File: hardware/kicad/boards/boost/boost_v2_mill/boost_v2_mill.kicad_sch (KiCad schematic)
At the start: 17 parts, among them J1 lager ind (5V), J2 V2 ud (10V), J3 PWM (isoleret), J4 drive +15V, M1 IRF530, U1 CNY17, U2 IR2110

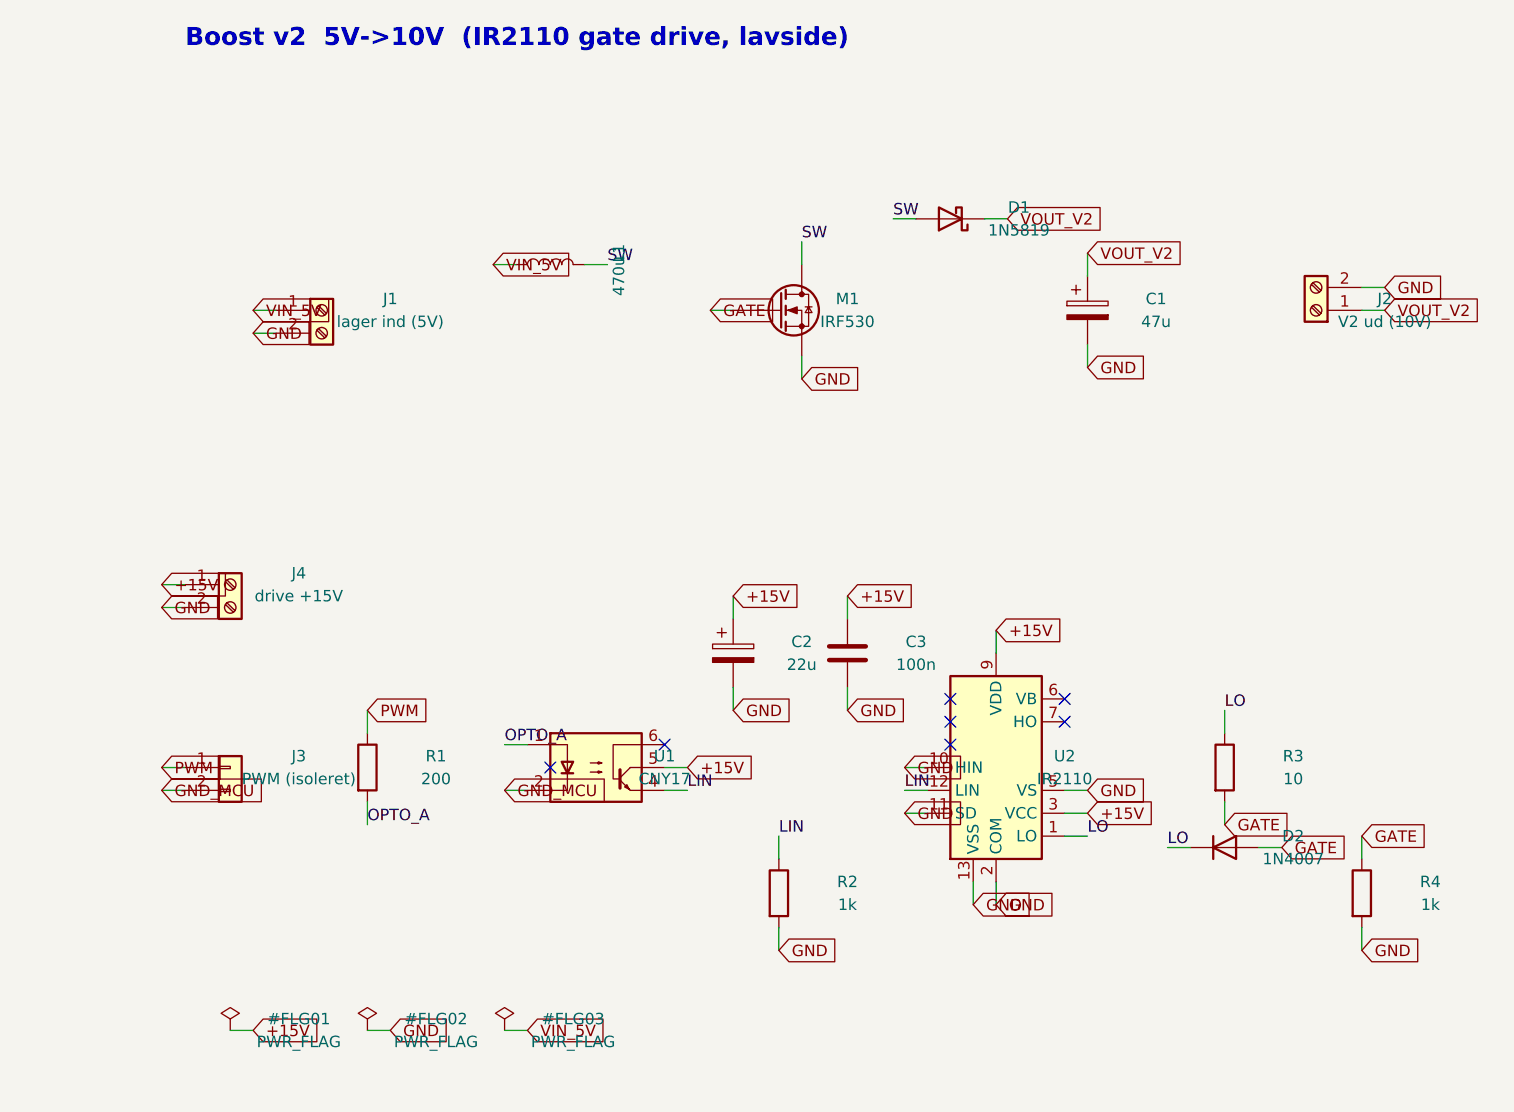
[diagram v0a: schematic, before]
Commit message: system PCB: lock double-sided CNC integration (Phase 0-2.2)
Set up the whole-system board as one double-sided CNC-milled PCB.

- system.kicad_pro: CNC double-sided netclass (clearance 1.0 mm, track 1.0 mm,
  hand-stitch via 2.4/1.0 mm) replacing the laser 0.8 mm rules
- interface contract (docs/superpowers/specs/2026-06-27-...) + rewritten
  label howto for the 5-board split-MCU integration
- split MCU: Arduino owns MPPT (PV INA219 + drives mppt_buck PWM at 5 V),
  C2000 runs motor-buck + boost PID; the two MCUs are fully independent
- current_sense (discrete) dropped; current sensing via PV INA219
- c2000_feedback: strip I-channels + PWM pass, keep 3 V-dividers
  (V1/LOAD/STORE -> ADC)
- hierarchical labels placed on the 5 boards (motor_power, motor_feedback,
  mppt_buck, boost_v2_mill, c2000_feedback) for the system top sheet
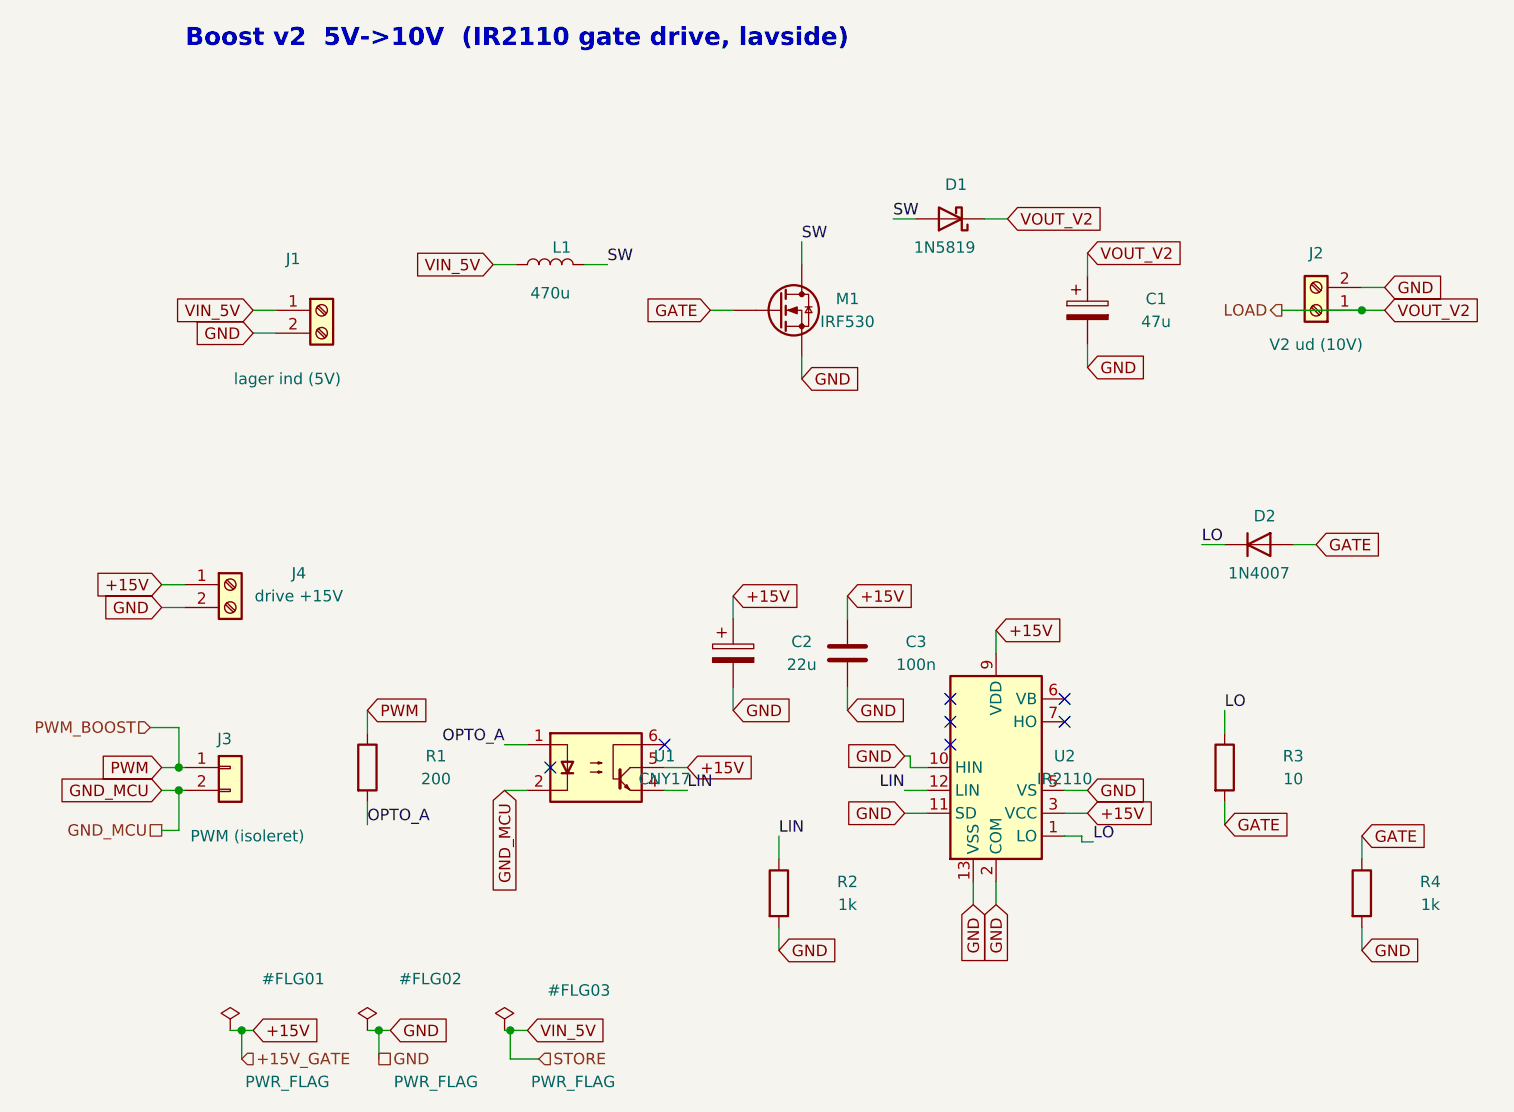
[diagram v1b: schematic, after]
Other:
- moved on the sheet: D2

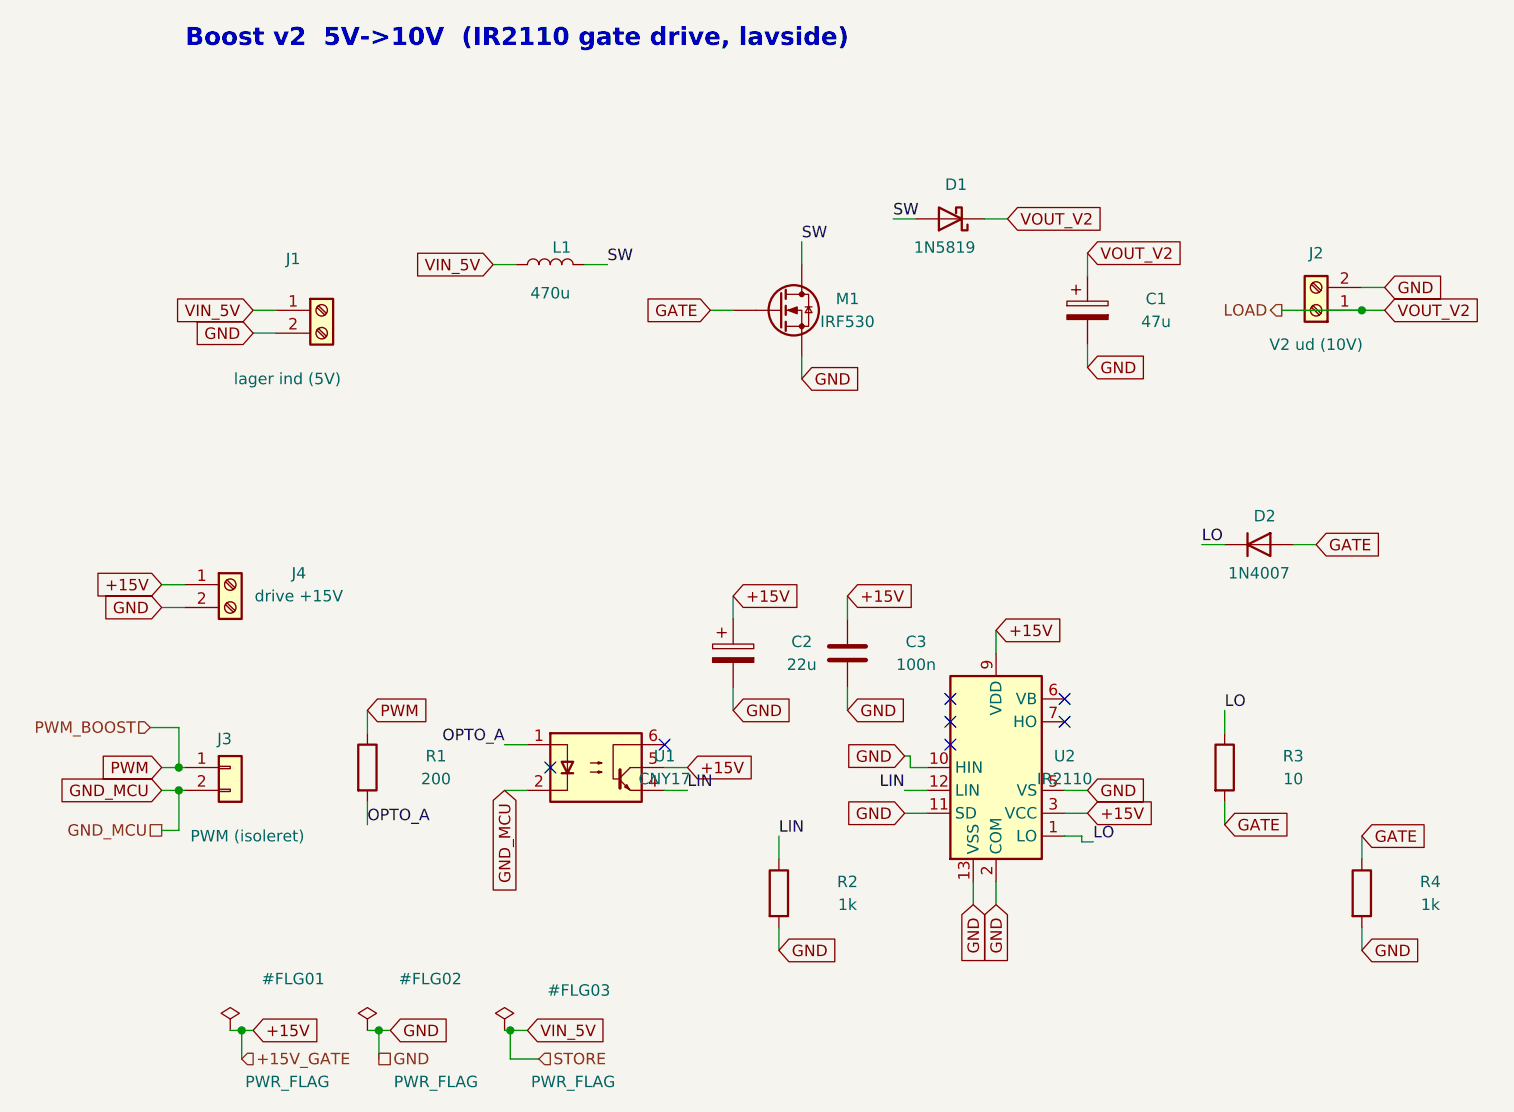
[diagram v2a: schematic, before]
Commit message: system: single edge-connector set + integrated board
- delete 22 redundant board-level I/O connectors (J201-207, J301-302,
  J401-404, J501-504, J601-605); on the monolithic board these are internal
  board-to-board nets (now copper traces) or duplicates of the top-level edge
  set. Nets carried by the hierarchical sheet pins; netlist re-verified.
- C212: real capacitor footprint, + on V1 (was a swap terminal)
- motor_feedback MCU-side powered from +5V_PWR (merged +5V_MCU)
- footprints assigned to all top-level connectors/probes (J_*, TP, R_STAR)
- system.kicad_pcb: integrated board pulled via Update-PCB-from-Schematic
- placement guide (PNG + PDF) + generator/patch scripts
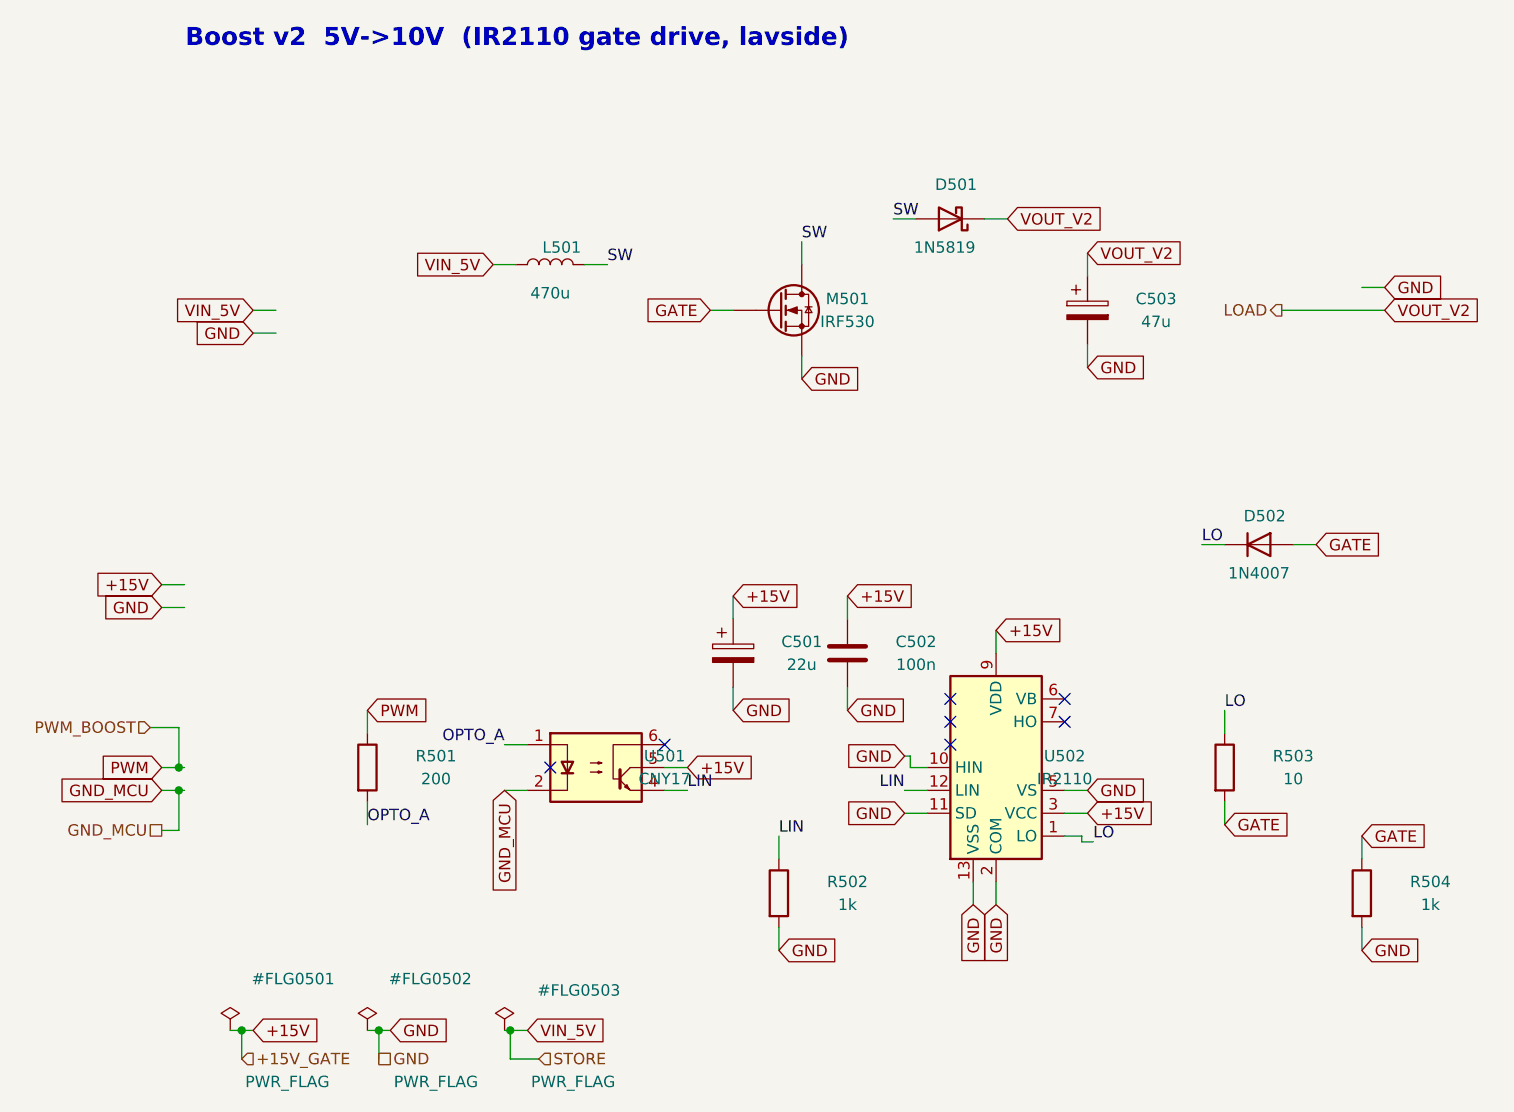
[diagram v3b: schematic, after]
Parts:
- removed J1: lager ind (5V), TerminalBlock:TerminalBlock_bornier-2_P5.08mm, symbol Connector:Screw_Terminal_01x02
- removed J2: V2 ud (10V), TerminalBlock:TerminalBlock_bornier-2_P5.08mm, symbol Connector:Screw_Terminal_01x02
- removed J3: PWM (isoleret), Connector_PinHeader_2.54mm:PinHeader_1x02_P2.54mm_Vertical, symbol Connector_Generic:Conn_01x02
- removed J4: drive +15V, TerminalBlock:TerminalBlock_bornier-2_P5.08mm, symbol Connector:Screw_Terminal_01x02
- renumbered C2 to C501, C3 to C502, C1 to C503, D1 to D501, D2 to D502, L1 to L501, M1 to M501, R1 to R501, R2 to R502, R3 to R503, R4 to R504, U1 to U501, U2 to U502
